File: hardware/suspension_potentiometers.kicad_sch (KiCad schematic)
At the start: 0 parts

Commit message: Add the Cube project
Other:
- title: (none) -> Suspension Potentiometers
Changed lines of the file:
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@@
   (paper "A4")
   (title_block
-    (date "2023-06-06")
+    (title "Suspension Potentiometers")
+    (date "2023-07-01")
     (rev "${REVISION}")
     (company "Author: I. Kajdan")
@@
     (stroke (width 0) (type default))
   )
-  (hierarchical_label "IN1" (shape input) (at 130.81 93.98 180) (fields_autoplaced)
+  (hierarchical_label "IN_L" (shape input) (at 130.81 93.98 180) (fields_autoplaced)
     (effects (font (size 1.27 1.27)) (justify right))
   )
-  (hierarchical_label "OUT1" (shape output) (at 162.56 93.98 0) (fields_autoplaced)
+  (hierarchical_label "OUT_L" (shape output) (at 162.56 93.98 0) (fields_autoplaced)
     (effects (font (size 1.27 1.27)) (justify left))
   )
-  (hierarchical_label "IN2" (shape input) (at 130.81 109.22 180) (fields_autoplaced)
+  (hierarchical_label "IN_R" (shape input) (at 130.81 109.22 180) (fields_autoplaced)
     (effects (font (size 1.27 1.27)) (justify right))
   )
-  (hierarchical_label "OUT2" (shape output) (at 162.56 109.22 0) (fields_autoplaced)
+  (hierarchical_label "OUT_R" (shape output) (at 162.56 109.22 0) (fields_autoplaced)
     (effects (font (size 1.27 1.27)) (justify left))
   )

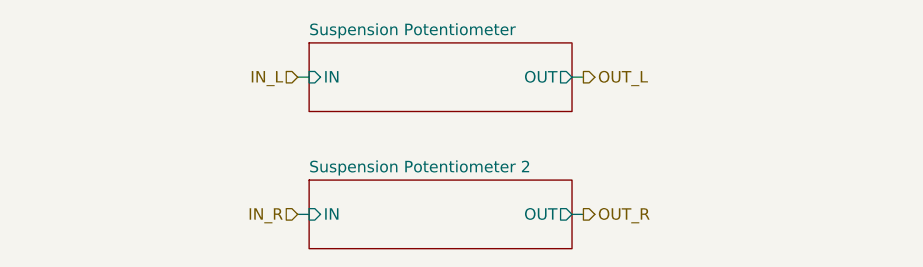
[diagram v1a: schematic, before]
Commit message: Improve the schematic
- add anti-aliasing filters
- rearrange the main connector signals
- improve the power filtering
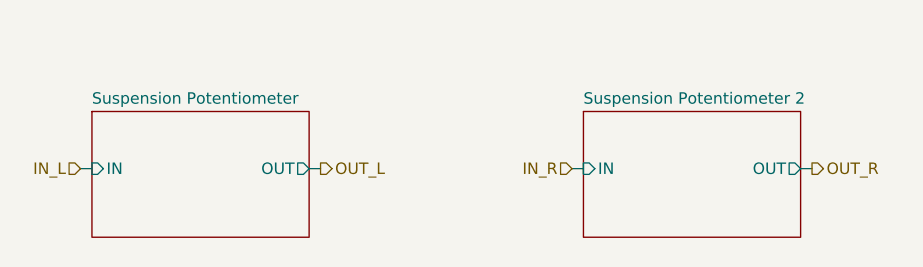
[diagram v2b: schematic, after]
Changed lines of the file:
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@@
     (comment 1 "Reviewer:")
   )
-  (wire (pts (xy 161.29 109.22) (xy 162.56 109.22))
+  (wire (pts (xy 186.69 104.14) (xy 187.96 104.14))
     (stroke (width 0) (type default))
   )
-  (wire (pts (xy 130.81 109.22) (xy 132.08 109.22))
+  (wire (pts (xy 161.29 104.14) (xy 162.56 104.14))
     (stroke (width 0) (type default))
   )
-  (wire (pts (xy 161.29 93.98) (xy 162.56 93.98))
+  (wire (pts (xy 132.08 104.14) (xy 133.35 104.14))
     (stroke (width 0) (type default))
   )
-  (wire (pts (xy 130.81 93.98) (xy 132.08 93.98))
+  (wire (pts (xy 106.68 104.14) (xy 107.95 104.14))
     (stroke (width 0) (type default))
   )
-  (hierarchical_label "IN_L" (shape input) (at 130.81 93.98 180) (fields_autoplaced)
+  (hierarchical_label "IN_L" (shape input) (at 106.68 104.14 180) (fields_autoplaced)
     (effects (font (size 1.27 1.27)) (justify right))
   )
-  (hierarchical_label "OUT_L" (shape output) (at 162.56 93.98 0) (fields_autoplaced)
+  (hierarchical_label "OUT_L" (shape output) (at 133.35 104.14 0) (fields_autoplaced)
     (effects (font (size 1.27 1.27)) (justify left))
   )
-  (hierarchical_label "IN_R" (shape input) (at 130.81 109.22 180) (fields_autoplaced)
+  (hierarchical_label "IN_R" (shape input) (at 161.29 104.14 180) (fields_autoplaced)
     (effects (font (size 1.27 1.27)) (justify right))
   )
-  (hierarchical_label "OUT_R" (shape output) (at 162.56 109.22 0) (fields_autoplaced)
+  (hierarchical_label "OUT_R" (shape output) (at 187.96 104.14 0) (fields_autoplaced)
     (effects (font (size 1.27 1.27)) (justify left))
   )
-  (sheet (at 132.08 105.41) (size 29.21 7.62) (fields_autoplaced)
+  (sheet (at 162.56 97.79) (size 24.13 13.97) (fields_autoplaced)
     (stroke (width 0.1524) (type solid))
     (fill (color 0 0 0 0.0000))
-    (property "Sheetname" "Suspension Potentiometer 2" (at 132.08 104.6984 0)
+    (property "Sheetname" "Suspension Potentiometer 2" (at 162.56 97.0784 0)
       (effects (font (size 1.27 1.27)) (justify left bottom))
     )
-    (property "Sheetfile" "suspension_potentiometer.kicad_sch" (at 132.08 113.6146 0)
+    (property "Sheetfile" "suspension_potentiometer.kicad_sch" (at 162.56 112.3446 0)
       (effects (font (size 1.27 1.27)) (justify left top) hide)
     )
-    (pin "IN" input (at 132.08 109.22 180)
+    (pin "IN" input (at 162.56 104.14 180)
       (effects (font (size 1.27 1.27)) (justify left))
     )
-    (pin "OUT" output (at 161.29 109.22 0)
+    (pin "OUT" output (at 186.69 104.14 0)
       (effects (font (size 1.27 1.27)) (justify right))
     )
@@
     )
   )
-  (sheet (at 132.08 90.17) (size 29.21 7.62) (fields_autoplaced)
+  (sheet (at 107.95 97.79) (size 24.13 13.97)
     (stroke (width 0.1524) (type solid))
     (fill (color 0 0 0 0.0000))
-    (property "Sheetname" "Suspension Potentiometer" (at 132.08 89.4584 0)
+    (property "Sheetname" "Suspension Potentiometer" (at 107.95 97.0784 0)
       (effects (font (size 1.27 1.27)) (justify left bottom))
     )
-    (property "Sheetfile" "suspension_potentiometer.kicad_sch" (at 132.08 98.3746 0)
+    (property "Sheetfile" "suspension_potentiometer.kicad_sch" (at 107.95 105.9946 0)
       (effects (font (size 1.27 1.27)) (justify left top) hide)
     )
-    (pin "IN" input (at 132.08 93.98 180)
+    (pin "IN" input (at 107.95 104.14 180)
       (effects (font (size 1.27 1.27)) (justify left))
     )
-    (pin "OUT" output (at 161.29 93.98 0)
+    (pin "OUT" output (at 132.08 104.14 0)
       (effects (font (size 1.27 1.27)) (justify right))
     )

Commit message: Set component values
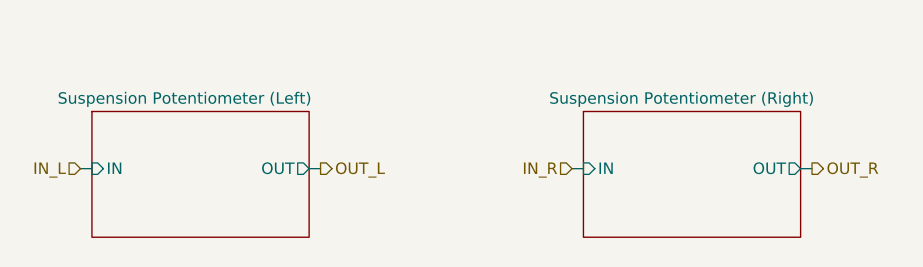
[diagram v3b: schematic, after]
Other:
- sheet Suspension Potentiometer renamed Suspension Potentiometer (Left)
- sheet Suspension Potentiometer 2 renamed Suspension Potentiometer (Right)
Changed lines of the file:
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@@
     (effects (font (size 1.27 1.27)) (justify left))
   )
-  (sheet (at 162.56 97.79) (size 24.13 13.97) (fields_autoplaced)
+  (sheet (at 162.56 97.79) (size 24.13 13.97)
     (stroke (width 0.1524) (type solid))
     (fill (color 0 0 0 0.0000))
-    (property "Sheetname" "Suspension Potentiometer 2" (at 162.56 97.0784 0)
+    (property "Sheetname" "Suspension Potentiometer (Right)" (at 158.75 97.0784 0)
       (effects (font (size 1.27 1.27)) (justify left bottom))
     )
@@
     (stroke (width 0.1524) (type solid))
     (fill (color 0 0 0 0.0000))
-    (property "Sheetname" "Suspension Potentiometer" (at 107.95 97.0784 0)
+    (property "Sheetname" "Suspension Potentiometer (Left)" (at 104.14 97.0784 0)
       (effects (font (size 1.27 1.27)) (justify left bottom))
     )
